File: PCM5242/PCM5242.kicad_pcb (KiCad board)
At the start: 2 copper layers, 70 x 50 mm, 27 parts, among them IC1 NCP163ASN330T1G, IC2 NCP163ASN330T1G, J1 Conn_01x04_Male, J2 Conn_01x12_Male, J3 d, U1 PCM5242, Y1 ASE-24.000MHZ-ET

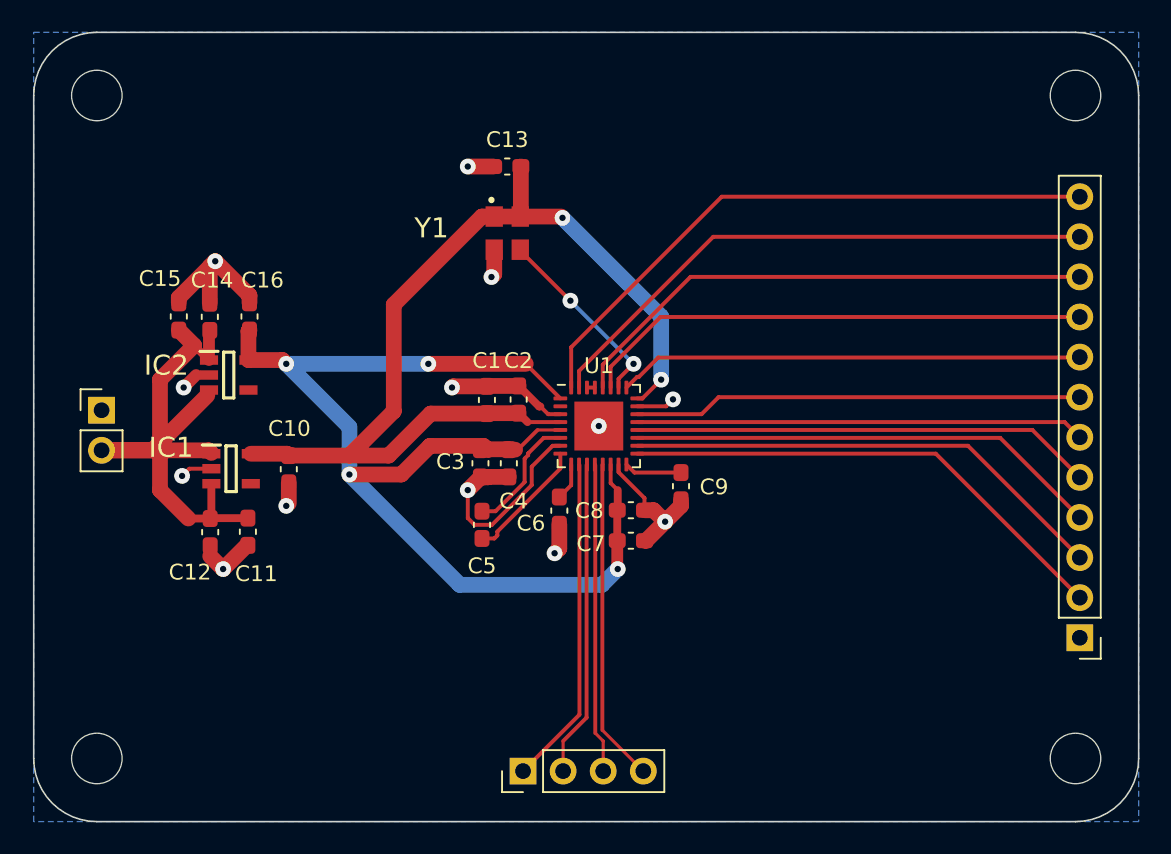
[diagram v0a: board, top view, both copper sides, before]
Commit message: 5242 PCB v.3 Update
Finished V.3. Should have correct footprints, pinouts for analog, good labeling.
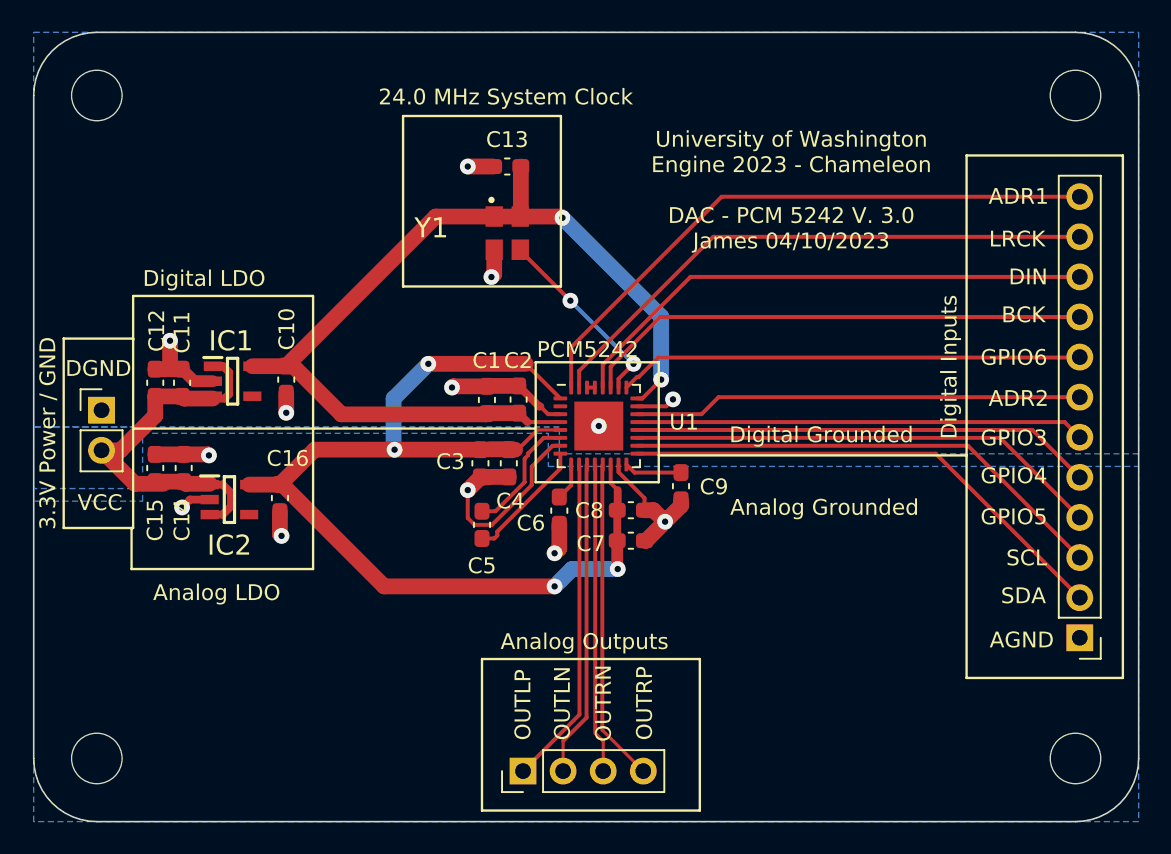
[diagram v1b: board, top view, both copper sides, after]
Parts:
- moved C16 11.7 mm to (98.6, 110.5), turned to 90 degrees
- moved C11 10.3 mm to (92.4, 103.2), turned to 90 degrees
- moved C12 10.1 mm to (90.7, 103.2), turned to 90 degrees
- moved C14 9.72 mm to (92.5, 108.6)
- moved C15 9.72 mm to (90.7, 108.6)
- moved IC2 7.89 mm to (95.4, 110.6)
- moved C10 5.68 mm to (99.0, 103.0)
- moved IC1 5.55 mm to (95.6, 103.1)
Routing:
- net VCC: track 38.1 -> 26.6 mm
- net AVDD: track 73.3 -> 67.7 mm
- net GND: track 57.2 -> 51.8 mm
- net DVDD: track 62.8 -> 60.0 mm
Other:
- board text added: "24.0 MHz System Clock"
- board text added: "3.3V Power / GND"
- board text added: "ADR1"
- board text added: "ADR2"
- board text added: "AGND"
- board text added: "Analog Grounded"
- board text added: "Analog LDO"
- board text added: "Analog Outputs"
- board text added: "BCK"
- board text added: "DGND"
- board text added: "DIN"
- board text added: "Digital Grounded"
- board text added: "Digital Inputs"
- board text added: "Digital LDO"
- board text added: "GPIO3"
- board text added: "GPIO4"
- board text added: "GPIO5"
- board text added: "GPIO6"
- board text added: "LRCK"
- board text added: "OUTLN"
- board text added: "OUTLP"
- board text added: "OUTRN"
- board text added: "OUTRP"
- board text added: "PCM5242"
- board text added: "SCL"
- board text added: "SDA"
- board text added: "University of Washington Engine 2023 - Chameleon DAC - PCM 5242 V. 3.0 James 04/10/2023"
- board text added: "VCC"
